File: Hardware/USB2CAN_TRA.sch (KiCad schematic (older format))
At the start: 24 parts, among them U4 STM32F042C6Tx, U5 MCP2551-I-SN, Y2 16 MHz

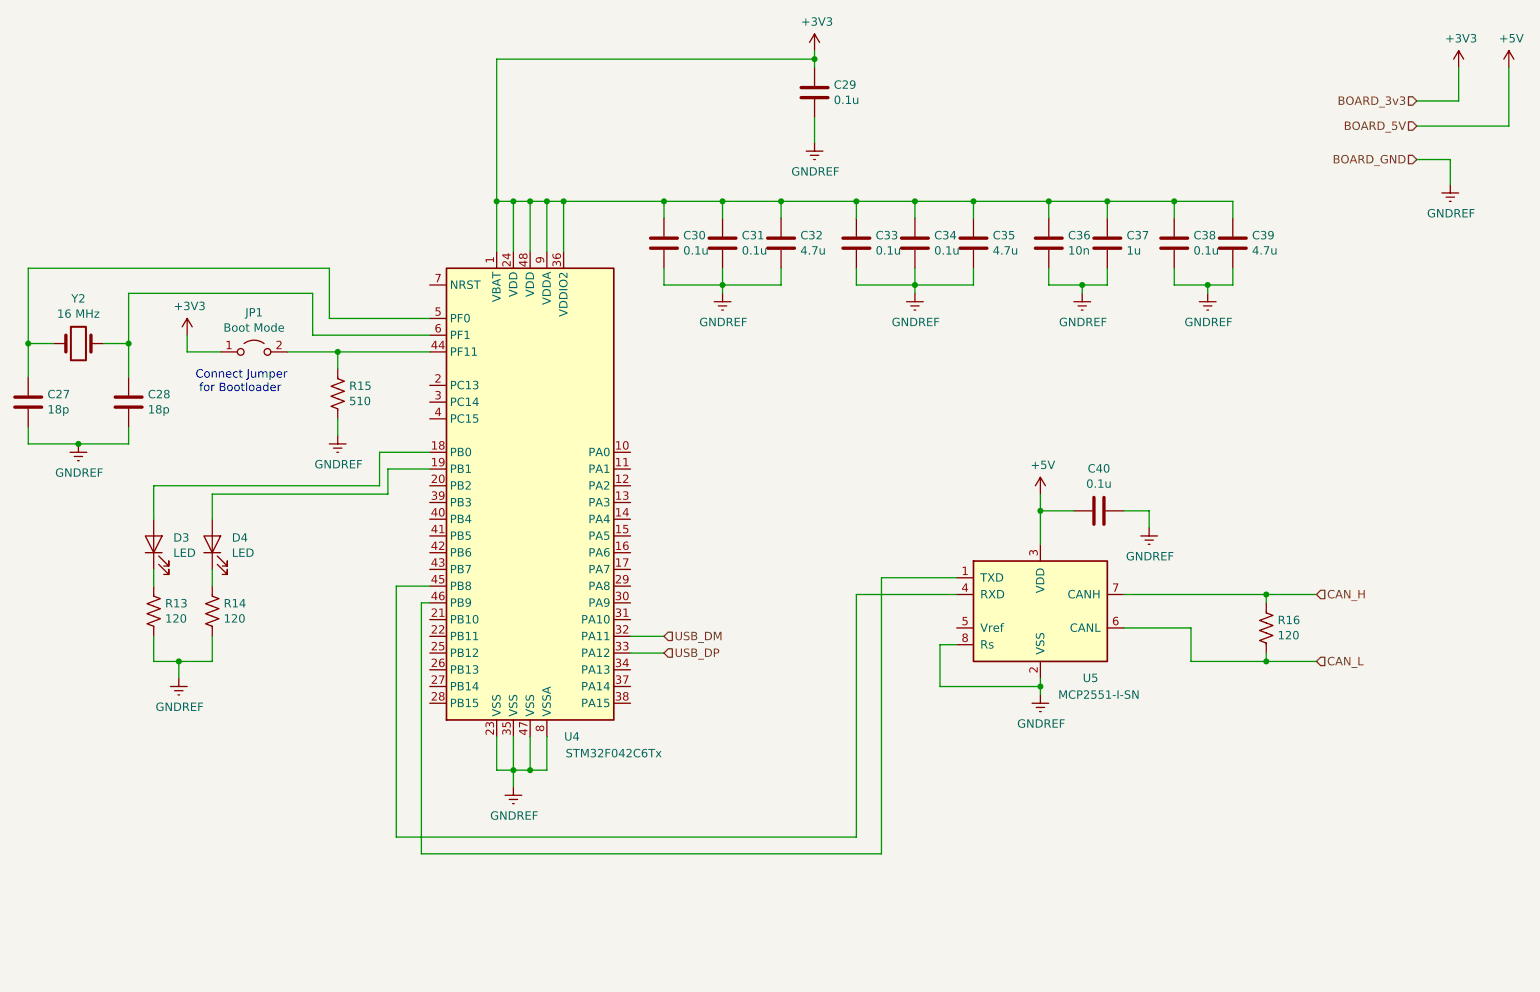
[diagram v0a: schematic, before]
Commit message: Added footprints to schematic symbols
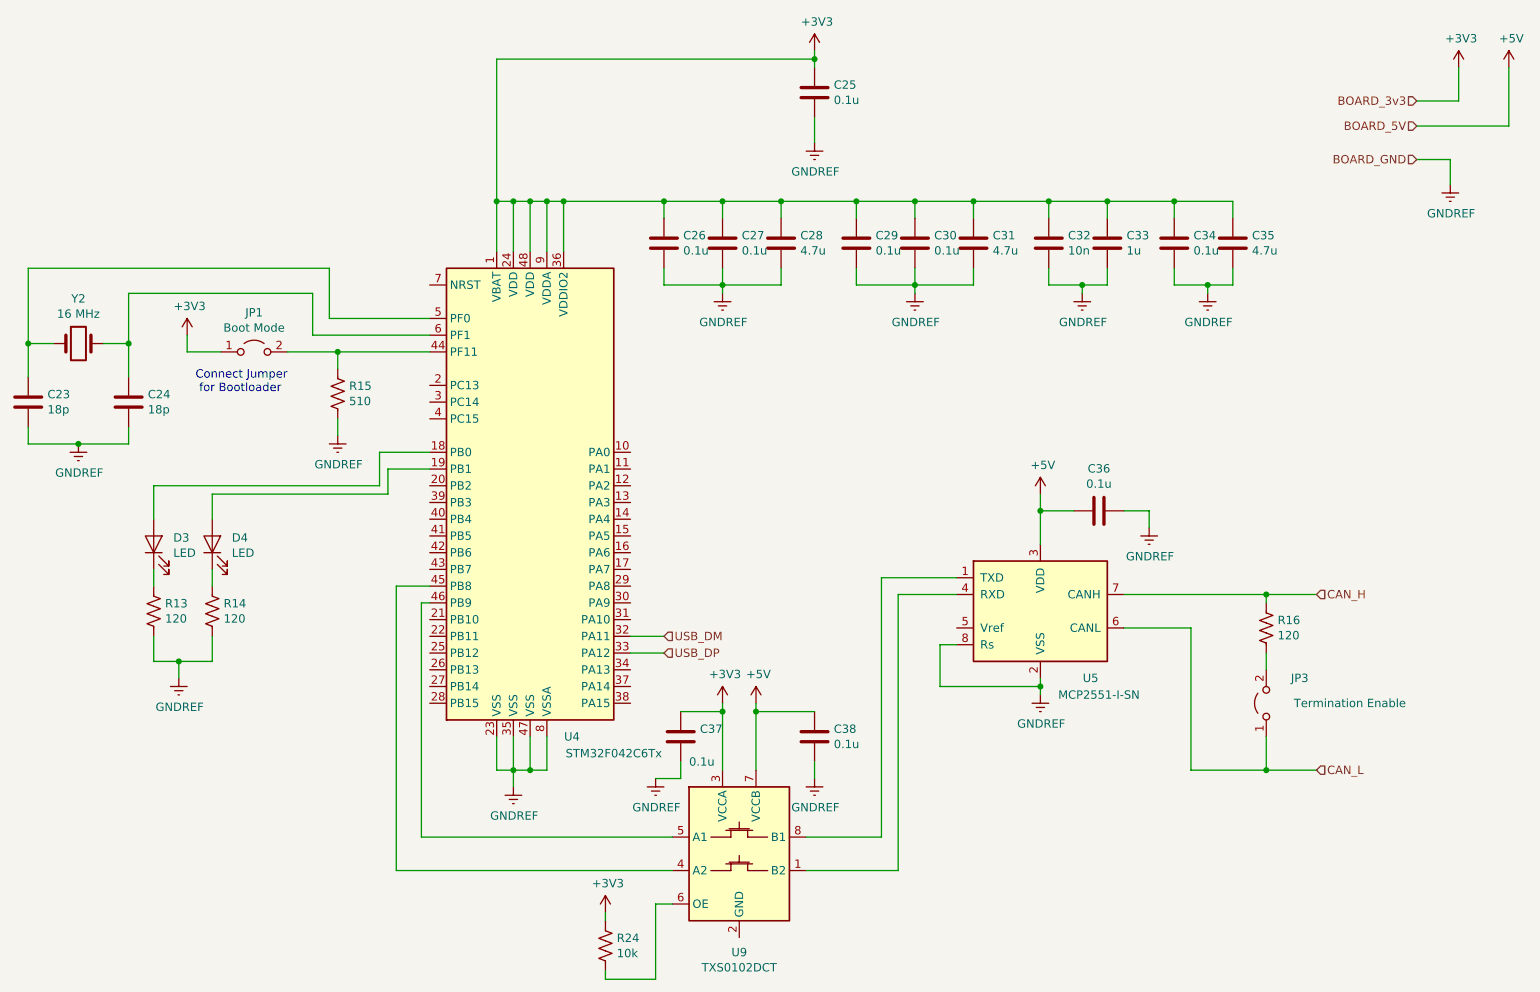
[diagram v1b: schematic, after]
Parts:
- removed C33, C34, C40: 0.1u, symbol Device:C
- removed C35: 4.7u, symbol Device:C
- added C23, C24: 18p, Capacitor_SMD:C_0603_1608Metric, symbol Device:C
- added C25, C26, C37, C38: 0.1u, Capacitor_SMD:C_0603_1608Metric, symbol Device:C
- added JP3: Termination Enable, Connector_PinHeader_1.27mm:PinHeader_2x01_P1.27mm_Vertical_SMD, symbol Jumper:Jumper_2_Open
- added R24: 10k, Resistor_SMD:R_1206_3216Metric, symbol Device:R_US
- added U9: TXS0102DCT, Package_SO:SSOP-8_2.95x2.8mm_P0.65mm, symbol Logic_LevelTranslator:TXS0102DCT
- C27: value 18p -> 0.1u; footprint (none) -> Capacitor_SMD:C_0603_1608Metric
- C28: value 18p -> 4.7u; footprint (none) -> Capacitor_SMD:C_0603_1608Metric
- C29, C30: footprint (none) -> Capacitor_SMD:C_0603_1608Metric
- C31: value 0.1u -> 4.7u; footprint (none) -> Capacitor_SMD:C_0603_1608Metric
- C32: value 4.7u -> 10n; footprint (none) -> Capacitor_SMD:C_0603_1608Metric
- C33: renamed from C37; footprint (none) -> Capacitor_SMD:C_0603_1608Metric
- C34: renamed from C38; footprint (none) -> Capacitor_SMD:C_0603_1608Metric
- C35: renamed from C39; footprint (none) -> Capacitor_SMD:C_0603_1608Metric
- C36: value 10n -> 0.1u; footprint (none) -> Capacitor_SMD:C_0603_1608Metric
- D3, D4: footprint (none) -> LED_SMD:LED_0805_2012Metric_Castellated
- JP1: footprint (none) -> Connector_PinHeader_1.27mm:PinHeader_2x01_P1.27mm_Vertical_SMD
- R13, R14, R15, R16: footprint (none) -> Resistor_SMD:R_1206_3216Metric
- Y2: footprint (none) -> Crystal:Crystal_SMD_2016-4Pin_2.0x1.6mm
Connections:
- net +3V3: now also C27.1, C28.1, C25.1, C26.1, C37.1, R24.2, U9.3 (VCCA); no longer C36.1
- net +5V: now also C36.2, C38.1, U9.7 (VCCB)
- net CAN_L: now also JP3.1 (A); no longer R16.2
- net GNDREF: now also C36.1, C23.2, C24.2, C25.2, C26.2, C37.2, C38.2; no longer C36.2
- net at U4.45 (PB8): now also U9.4 (A2); no longer U5.4 (RXD)
- net at U4.46 (PB9): now also U9.5 (A1); no longer U5.1 (TXD)
- net at U4.5 (PF0), Y2.1: now also C23.1; no longer C27.1
- net at U4.6 (PF1), Y2.2: now also C24.1; no longer C28.1
- new net: JP3.2 (B), R16.2
- new net: U5.1 (TXD), U9.8 (B1)
- new net: U5.4 (RXD), U9.1 (B2)
- new net: R24.1, U9.6 (OE)
